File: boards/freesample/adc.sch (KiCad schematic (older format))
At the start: 0 parts

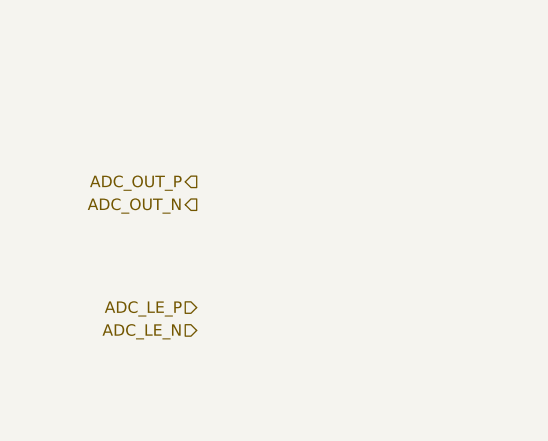
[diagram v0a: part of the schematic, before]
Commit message: Continued initial schematic capture
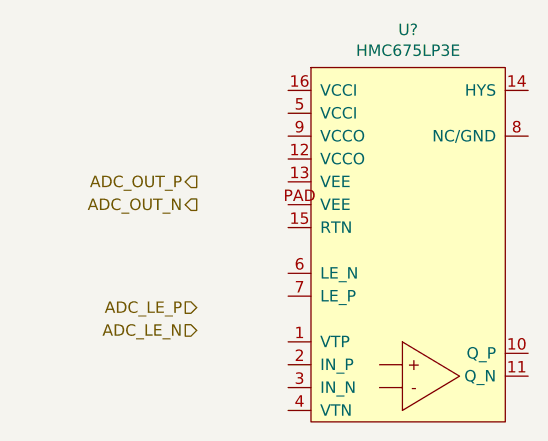
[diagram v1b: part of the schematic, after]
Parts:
- added U?: HMC675LP3E, symbol analog-azonenberg:HMC675LP3E
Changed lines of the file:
@@
 $Descr A4 11693 8268
 encoding utf-8
-Sheet 7 11
+Sheet 7 12
 Title "FREESAMPLE Oscilloscope"
-Date "2018-12-15"
+Date "2018-12-17"
 Rev "0.1"
 Comp "Andrew D. Zonenberg / Antikernel Labs"
@@
 Text HLabel 5800 2650 0    50   Input ~ 0
 ADC_LE_N
+$Comp
+L analog-azonenberg:HMC675LP3E U?
+U 1 1 5C3D1D95
+P 6300 3050
+F 0 "U?" H 6725 4765 50  0000 C CNN
+F 1 "HMC675LP3E" H 6725 4674 50  0000 C CNN
+F 2 "" H 6300 3050 50  0001 C CNN
+F 3 "" H 6300 3050 50  0001 C CNN
+	1    6300 3050
+	1    0    0    -1
+$EndComp
 $EndSCHEMATC

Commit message: Continued work on schematic capture
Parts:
- added C133, C134, C135, C136, C137, C144: 100 pF, symbol device:C
- added C138, C139, C140: 330 pF, symbol device:C
- added C141, C142, C143: 4.7 uF, symbol device:C
- added R18: DNP, symbol device:R
- gave numbers to parts that had none: 1
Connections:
- net 1V8: now also U8.12 (VCCO), U8.9 (VCCO), C134.1, C137.1, C140.1, C143.1
- net 3V0_N: now also U8.13 (VEE), U8.PAD (VEE), C135.1, C138.1, C141.1
- net 3V3: now also U8.16 (VCCI), U8.5 (VCCI), C133.1, C136.1, C139.1, C142.1, C144.1
- net ADC_DIN: now also U8.2 (IN_P)
- net ADC_LE_N: now also U8.6 (LE_N)
- net ADC_LE_P: now also U8.7 (LE_P)
- net ADC_OUT_N: now also U8.11 (Q_N)
- net ADC_OUT_P: now also U8.10 (Q_P)
- net ADC_VT: now also U8.3 (IN_N)
- net GND: now also U8.1 (VTP), U8.15 (RTN), U8.8 (NC/GND), C133.2, C134.2, C135.2, C136.2, C137.2, C138.2, C139.2, C140.2, C141.2, C142.2, C143.2, C144.2, R18.2
- net at U8.4 (VTN): now also R18.1
- no-connect marks 0 -> 1
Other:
- moved on the sheet: U8

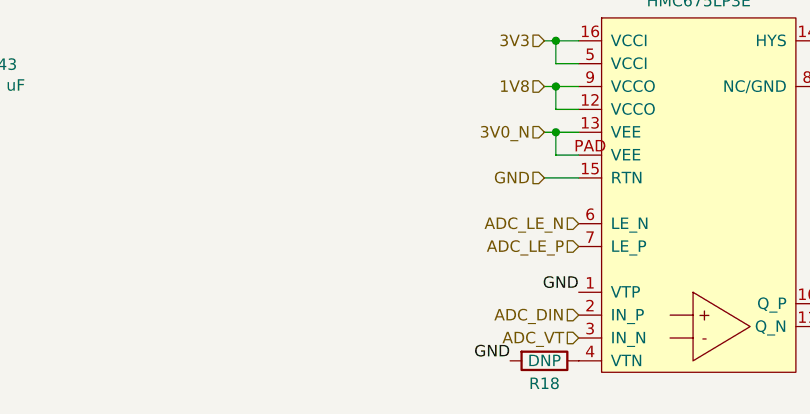
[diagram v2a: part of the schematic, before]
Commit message: Continued work on FREESAMPLE schematic including PSU.
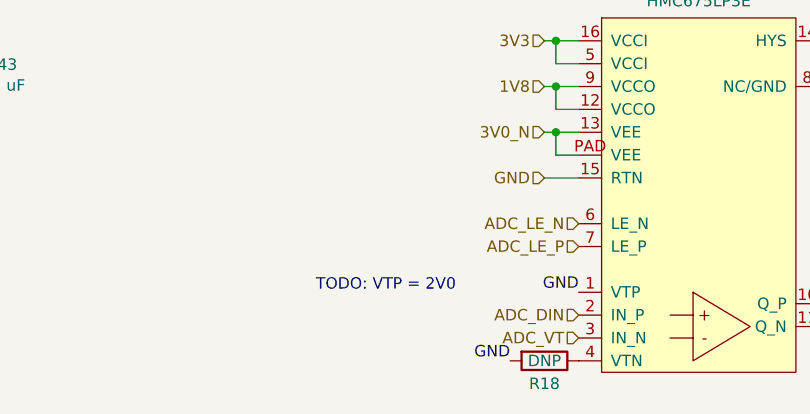
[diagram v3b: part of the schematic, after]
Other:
- note added: "TODO: VTP = 2V0"
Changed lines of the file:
@@
 Sheet 7 12
 Title "FREESAMPLE Oscilloscope"
-Date "2018-12-17"
+Date "2019-02-23"
 Rev "0.1"
 Comp "Andrew D. Zonenberg / Antikernel Labs"
@@
 Text Label 6300 1550 0    50   ~ 0
 GND
+Text Notes 4100 2450 0    50   ~ 0
+TODO: VTP = 2V0
 $EndSCHEMATC

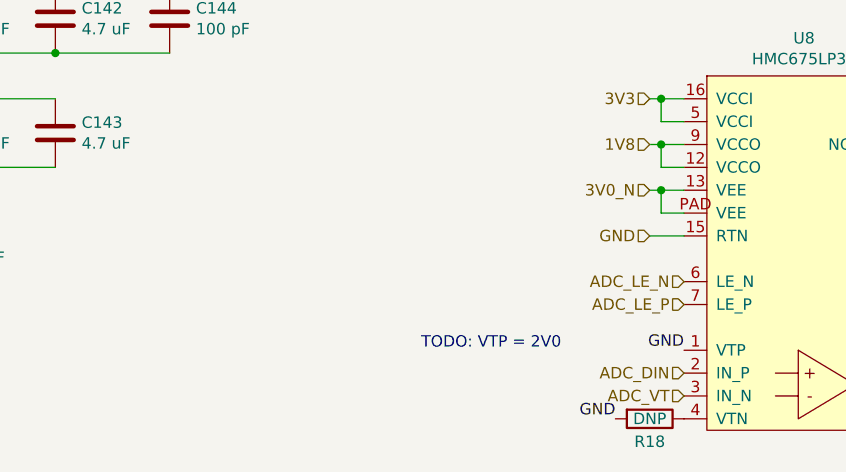
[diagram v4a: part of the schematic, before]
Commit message: Continued schematic capture work. Hooked up most SoM connectors.
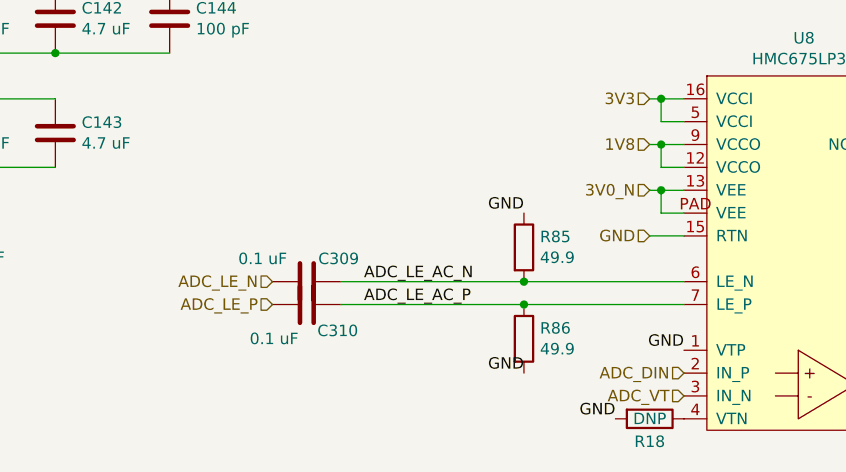
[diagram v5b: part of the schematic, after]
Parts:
- added C309, C310: 0.1 uF, symbol device:C
- added R85, R86: 49.9, symbol device:R
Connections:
- net ADC_LE_N: now also C309.2; no longer U8.6 (LE_N)
- net ADC_LE_P: now also C310.2; no longer U8.7 (LE_P)
- net GND: now also R85.1, R86.2
- new net ADC_LE_AC_N: C309.1, R85.2, U8.6 (LE_N)
- new net ADC_LE_AC_P: C310.1, R86.1, U8.7 (LE_P)
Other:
- note removed: "TODO: VTP = 2V0"
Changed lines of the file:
@@
 Sheet 7 12
 Title "FREESAMPLE Oscilloscope"
-Date "2019-02-26"
+Date "2019-03-10"
 Rev "0.1"
 Comp "Andrew D. Zonenberg / Antikernel Labs"
-Comment1 ""
+Comment1 "Ready for review"
 Comment2 ""
 Comment3 ""
@@
 Text HLabel 6300 2600 2    50   Output ~ 0
 ADC_OUT_N
-Text HLabel 5250 2250 0    50   Input ~ 0
+Text HLabel 3450 2250 0    50   Input ~ 0
 ADC_LE_P
-Text HLabel 5250 2150 0    50   Input ~ 0
+Text HLabel 3450 2150 0    50   Input ~ 0
 ADC_LE_N
 $Comp
@@
 Text Label 6300 1550 0    50   ~ 0
 GND
-Text Notes 4100 2450 0    50   ~ 0
-TODO: VTP = 2V0
+$Comp
+L device:C C?
+U 1 1 5CB77A5B
+P 3600 2150
+AR Path="/5C0E404A/5CB77A5B" Ref="C?"  Part="1"
+AR Path="/5C23AE1C/5CB77A5B" Ref="C?"  Part="1"
+AR Path="/5C20498F/5CB77A5B" Ref="C309"  Part="1"
+F 0 "C309" V 3500 2200 50  0000 L CNN
+F 1 "0.1 uF" V 3500 1850 50  0000 L CNN
+F 2 "" H 3638 2000 50  0001 C CNN
+F 3 "" H 3600 2150 50  0001 C CNN
+	1    3600 2150
+	0    1    1    0
+$EndComp
+$Comp
+L device:C C?
+U 1 1 5CB785A9
+P 3600 2250
+AR Path="/5C0E404A/5CB785A9" Ref="C?"  Part="1"
+AR Path="/5C23AE1C/5CB785A9" Ref="C?"  Part="1"
+AR Path="/5C20498F/5CB785A9" Ref="C310"  Part="1"
+F 0 "C310" V 3715 2296 50  0000 L CNN
+F 1 "0.1 uF" V 3750 2000 50  0000 L CNN
+F 2 "" H 3638 2100 50  0001 C CNN
+F 3 "" H 3600 2250 50  0001 C CNN
+	1    3600 2250
+	0    1    1    0
+$EndComp
+Wire Wire Line
+	4550 2150 3750 2150
+Text Label 3850 2150 0    50   ~ 0
+ADC_LE_AC_N
+Text Label 3850 2250 0    50   ~ 0
+ADC_LE_AC_P
+$Comp
+L device:R R85
+U 1 1 5CB822E8
+P 4550 2000
+F 0 "R85" H 4620 2046 50  0000 L CNN
+F 1 "49.9" H 4620 1955 50  0000 L CNN
+F 2 "" V 4480 2000 50  0001 C CNN
+F 3 "" H 4550 2000 50  0001 C CNN
+	1    4550 2000
+	1    0    0    -1
+$EndComp
+Wire Wire Line
+	4550 2150 5250 2150
+Connection ~ 4550 2150
+Wire Wire Line
+	3750 2250 4550 2250
+Text Label 4550 1850 2    50   ~ 0
+GND
+$Comp
+L device:R R86
+U 1 1 5CB83E21
+P 4550 2400
+F 0 "R86" H 4620 2446 50  0000 L CNN
+F 1 "49.9" H 4620 2355 50  0000 L CNN
+F 2 "" V 4480 2400 50  0001 C CNN
+F 3 "" H 4550 2400 50  0001 C CNN
+	1    4550 2400
+	1    0    0    -1
+$EndComp
+Connection ~ 4550 2250
+Wire Wire Line
+	4550 2250 5250 2250
+Text Label 4550 2550 2    50   ~ 0
+GND
 $EndSCHEMATC

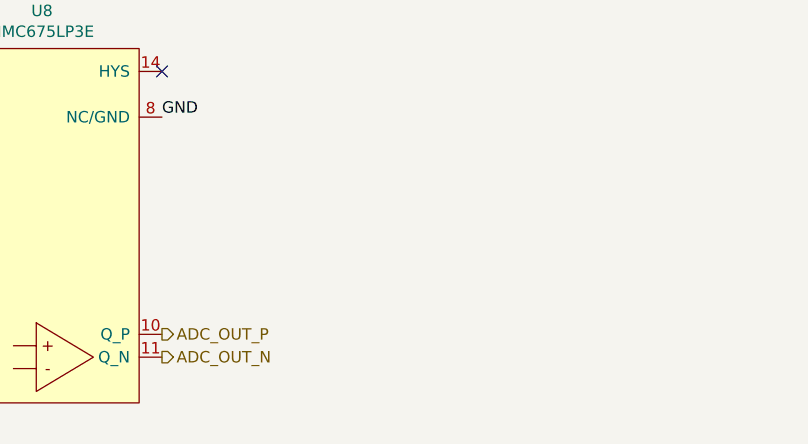
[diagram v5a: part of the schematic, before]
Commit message: Lots of ERC fixes, added CML-to-LVDS buffers for FPGA input signals
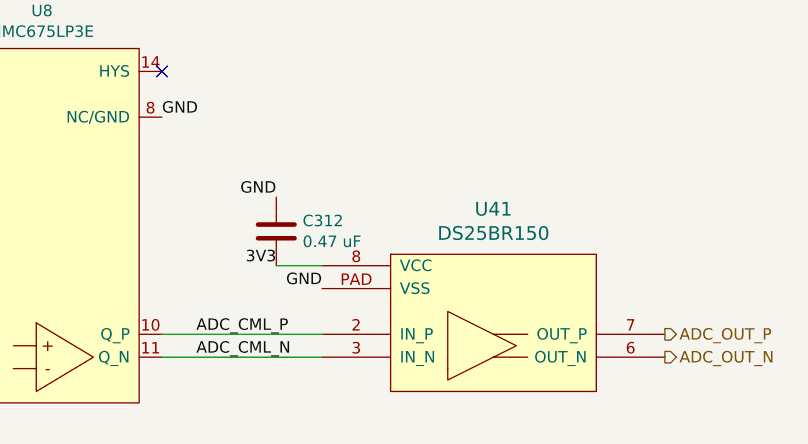
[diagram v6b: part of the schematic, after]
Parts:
- added C312: 0.47 uF, symbol device:C
- added U41: DS25BR150, symbol special-azonenberg:DS25BR150
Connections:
- net 3V3: now also C312.2, U41.8 (VCC)
- net ADC_OUT_N: now also U41.6 (OUT_N); no longer U8.11 (Q_N)
- net ADC_OUT_P: now also U41.7 (OUT_P); no longer U8.10 (Q_P)
- net GND: now also C312.1, U41.PAD (VSS)
- new net ADC_CML_N: U41.3 (IN_N), U8.11 (Q_N)
- new net ADC_CML_P: U41.2 (IN_P), U8.10 (Q_P)
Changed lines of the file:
@@
 Text HLabel 5100 1550 0    50   Input ~ 0
 1V8
-Text HLabel 6300 2500 2    50   Output ~ 0
+Text HLabel 8500 2500 2    50   Output ~ 0
 ADC_OUT_P
-Text HLabel 6300 2600 2    50   Output ~ 0
+Text HLabel 8500 2600 2    50   Output ~ 0
 ADC_OUT_N
 Text HLabel 3450 2250 0    50   Input ~ 0
@@
 Text Label 4550 2550 2    50   ~ 0
 GND
+$Comp
+L special-azonenberg:DS25BR150 U?
+U 1 1 5D17E9C8
+P 7300 2750
+AR Path="/5C15809A/5D17E9C8" Ref="U?"  Part="1"
+AR Path="/5C20498F/5D17E9C8" Ref="U41"  Part="1"
+F 0 "U41" H 7750 3547 60  0000 C CNN
+F 1 "DS25BR150" H 7750 3441 60  0000 C CNN
+F 2 "" H 7300 2750 60  0001 C CNN
+F 3 "" H 7300 2750 60  0001 C CNN
+	1    7300 2750
+	1    0    0    -1
+$EndComp
+Text Label 6800 2200 2    50   ~ 0
+3V3
+Text Label 7000 2300 2    50   ~ 0
+GND
+$Comp
+L device:C C?
+U 1 1 5D17E9D2
+P 6800 2050
+AR Path="/5C15809A/5D17E9D2" Ref="C?"  Part="1"
+AR Path="/5C20498F/5D17E9D2" Ref="C312"  Part="1"
+F 0 "C312" H 6915 2096 50  0000 L CNN
+F 1 "0.47 uF" H 6915 2005 50  0000 L CNN
+F 2 "" H 6838 1900 50  0001 C CNN
+F 3 "" H 6800 2050 50  0001 C CNN
+	1    6800 2050
+	1    0    0    -1
+$EndComp
+Wire Wire Line
+	6800 2200 7000 2200
+Text Label 6800 1900 2    50   ~ 0
+GND
+Wire Wire Line
+	6300 2500 7000 2500
+Wire Wire Line
+	7000 2600 6300 2600
+Text Label 6450 2500 0    50   ~ 0
+ADC_CML_P
+Text Label 6450 2600 0    50   ~ 0
+ADC_CML_N
 $EndSCHEMATC

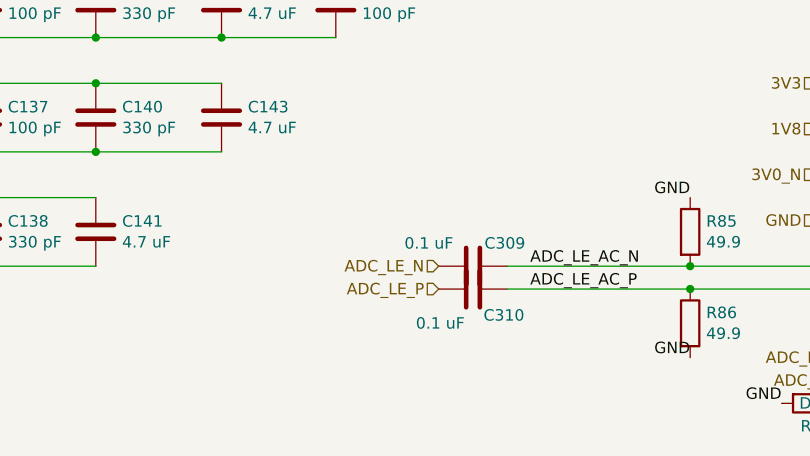
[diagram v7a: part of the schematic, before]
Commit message: Specified part number for AC coupling caps
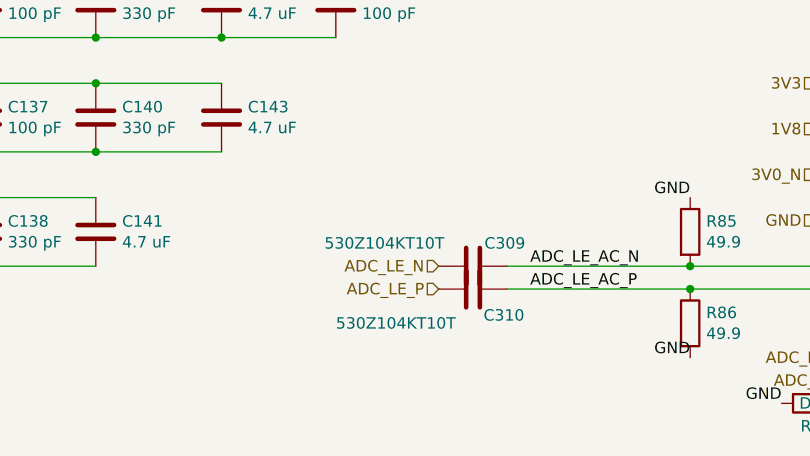
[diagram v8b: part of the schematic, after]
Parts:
- C309, C310: value 0.1 uF -> 530Z104KT10T
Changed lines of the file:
@@
 Sheet 7 12
 Title "FREESAMPLE Oscilloscope"
-Date "2019-03-11"
+Date "2019-03-13"
 Rev "0.1"
 Comp "Andrew D. Zonenberg / Antikernel Labs"
 Comment1 "Ready for review"
-Comment2 ""
+Comment2 "Ready for review"
 Comment3 ""
 Comment4 ""
@@
 AR Path="/5C20498F/5CB77A5B" Ref="C309"  Part="1"
 F 0 "C309" V 3500 2200 50  0000 L CNN
-F 1 "0.1 uF" V 3500 1850 50  0000 L CNN
+F 1 "530Z104KT10T" V 3500 1500 50  0000 L CNN
 F 2 "" H 3638 2000 50  0001 C CNN
 F 3 "" H 3600 2150 50  0001 C CNN
@@
 AR Path="/5C20498F/5CB785A9" Ref="C310"  Part="1"
 F 0 "C310" V 3715 2296 50  0000 L CNN
-F 1 "0.1 uF" V 3750 2000 50  0000 L CNN
+F 1 "530Z104KT10T" V 3750 1650 50  0000 L CNN
 F 2 "" H 3638 2100 50  0001 C CNN
 F 3 "" H 3600 2250 50  0001 C CNN
